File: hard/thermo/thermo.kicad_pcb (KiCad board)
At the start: 2 copper layers, 35 x 30 mm, 26 parts, among them J2 Conn_ARM_JTAG_SWD_10, J3 A-1JB, U2 nRF52832-QFxx, U3 Si7021-A20, Y1 XRCGB32M000F1H01R0, Y2 SC20S-9PF10PPM

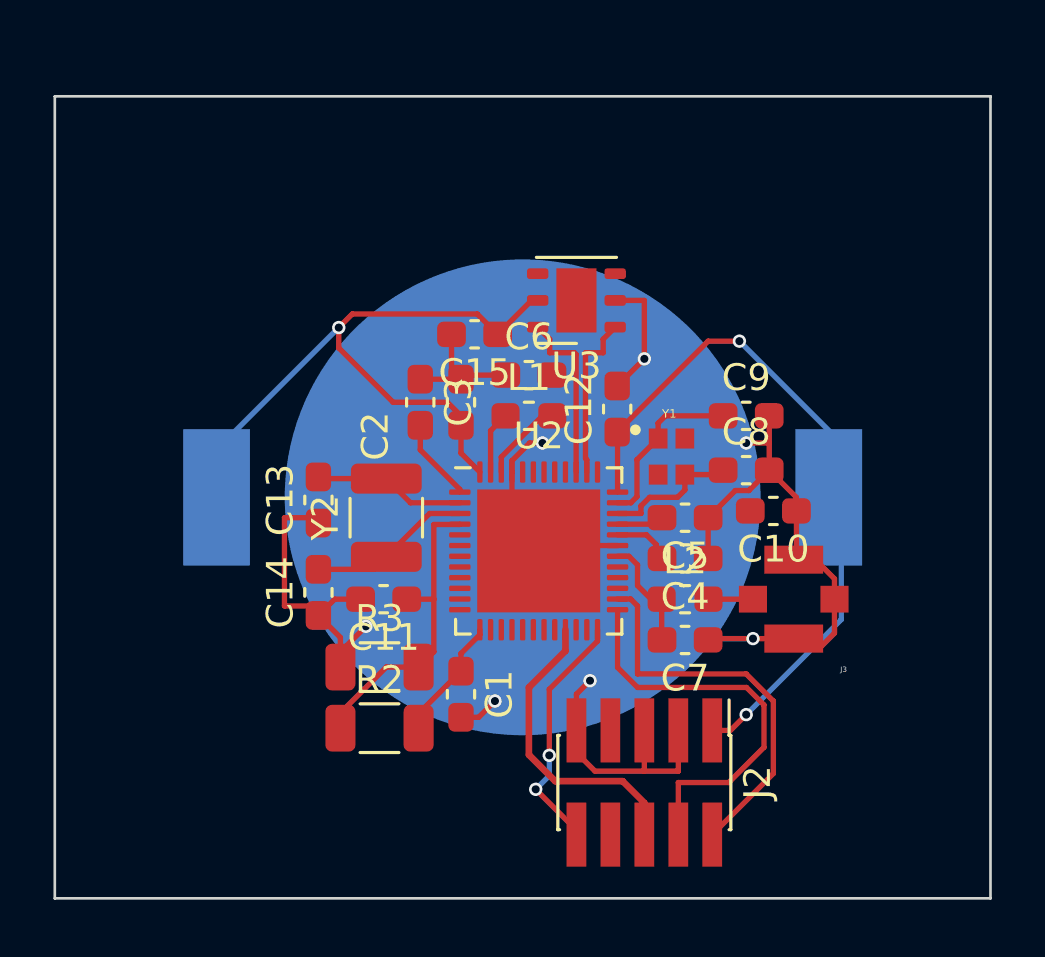
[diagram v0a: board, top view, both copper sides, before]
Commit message: - don't bother with >3.6V batt input - final layout
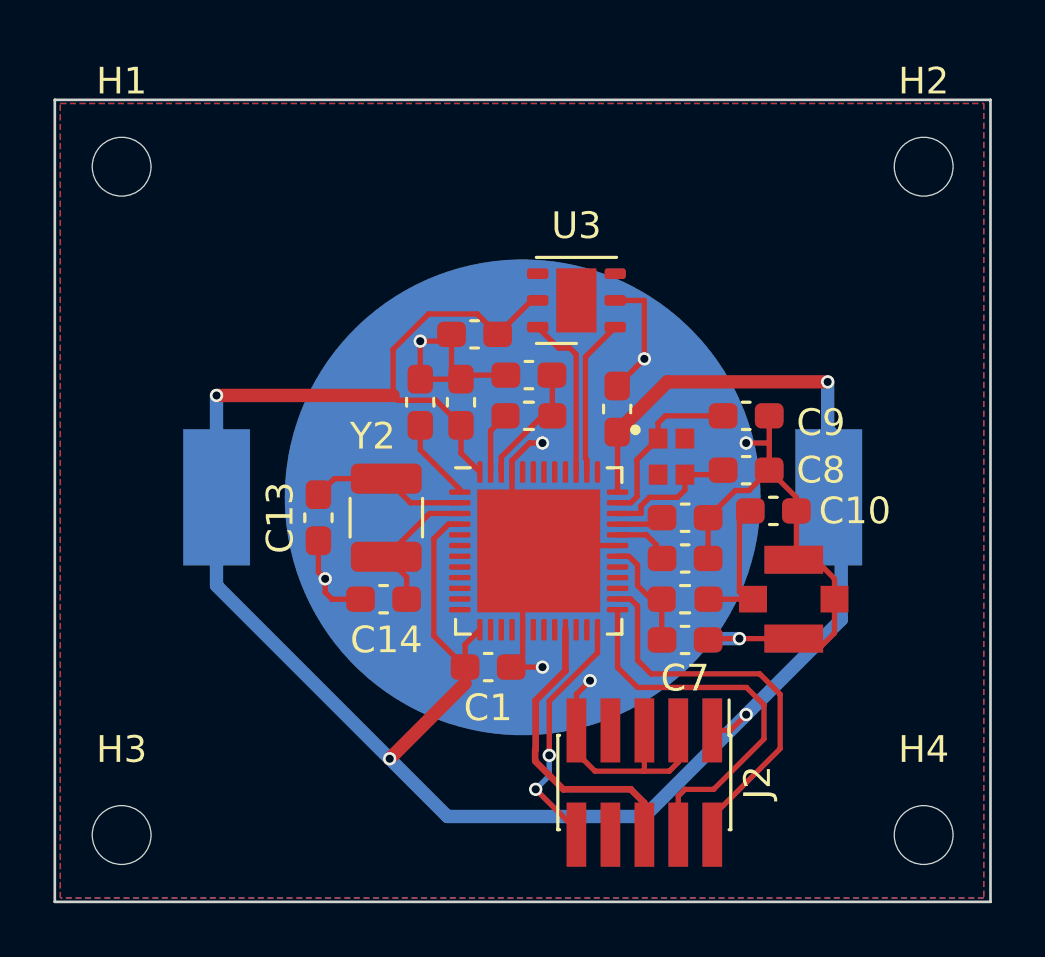
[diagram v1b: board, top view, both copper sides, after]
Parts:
- removed C11: 10n, Capacitor_SMD:C_0603_1608Metric_Pad1.08x0.95mm_HandSolder
- removed R2, R3: 1M, Resistor_SMD:R_1206_3216Metric
- added H1: MountingHole, MountingHole:MountingHole_2.2mm_M2, F.Cu at (142.5, 74.5)
- added H2: MountingHole, MountingHole:MountingHole_2.2mm_M2, F.Cu at (172.5, 74.5)
- added H3: MountingHole, MountingHole:MountingHole_2.2mm_M2, F.Cu at (142.5, 99.5)
- added H4: MountingHole, MountingHole:MountingHole_2.2mm_M2, F.Cu at (172.5, 99.5)
- moved C14 2.45 mm to (152.3, 90.7), turned to 0 degrees
- moved C1 1.44 mm to (156.2, 93.2), turned to 0 degrees
- moved C13 0.66 mm to (149.9, 87.6)
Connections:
- U2 pad 17: unconnected-(U2-P0.14-Pad17) -> GND
- U2 pad 4: Net-(U2-P0.02/AIN0) -> +BATT
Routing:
- net +BATT: track 56.7 -> 91.7 mm, vias 3 -> 4
- net Net-(U2-P0.02/AIN0): track 11.8 -> 0.00 mm
- net GND: track 74.7 -> 70.0 mm, vias 7 -> 8
- net Net-(C10-Pad2): track 2.06 -> 4.97 mm
- net Net-(U2-DEC4): track 3.11 -> 4.64 mm
- net Net-(U2-P0.01/XL2): track 6.16 -> 5.32 mm
- added copper zone on B.Cu, net GND
- added copper zone on F.Cu, net GND

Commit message: silk screen touch-ups
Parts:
- J2: value Conn_ARM_JTAG_SWD_10 -> SWD
- J3: value A-1JB -> ANT U.FL
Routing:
- net GND: track 70.0 -> 76.2 mm
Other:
- board text added: "Thermo v1.0"

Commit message: - adding 3D models for nRF chip and Battery holder - stop tracking fp-info-cache file
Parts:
- BT1: value BAT-HLD-001 -> CR2032
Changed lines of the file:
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@@
     (pad "49" smd rect (at 0 0) (size 4.6 4.6) (layers "F.Cu" "F.Mask")
       (net 1 "GND") (pinfunction "VSS") (pintype "passive"))
-    (model "${KICAD6_3DMODEL_DIR}/Package_DFN_QFN.3dshapes/QFN-48-1EP_6x6mm_P0.4mm_EP4.6x4.6mm.wrl"
+    (model "${KICAD6_3DMODEL_DIR}/Package_DFN_QFN.3dshapes/QFN-48-1EP_6x6mm_Pitch0.4mm_EP4.66x4.66mm.wrl"
       (offset (xyz 0 0 0))
       (scale (xyz 1 1 1))
@@
     (property "Sheetname" "")
     (attr smd)
-    (fp_text reference "BT1" (at -6.055 10.389) (layer "B.SilkS")
+    (fp_text reference "BT1" (at -6.055 10.389) (layer "B.SilkS") hide
         (effects (font (size 1.4 1.4) (thickness 0.15)) (justify mirror))
     )
-    (fp_text value "BAT-HLD-001" (at 2.835 -10.389) (layer "B.Fab")
+    (fp_text value "CR2032" (at -8.616 10.668) (layer "B.SilkS")
         (effects (font (size 1.4 1.4) (thickness 0.15)) (justify mirror))
     )
@@
     (pad "P2" smd rect (at 11.45 0 180) (size 2.5 5.1) (layers "B.Cu" "B.Paste" "B.Mask")
       (net 2 "+BATT") (pintype "passive") (solder_mask_margin 0.102))
+    (model "/Users/dkv/Downloads/BAT-HLD-001/BAT-HLD-001.step"
+      (offset (xyz 0 0 0))
+      (scale (xyz 1 1 1))
+      (rotate (xyz -90 0 180))
+    )
   )
   (gr_rect (start 140 72) (end 175 102)
